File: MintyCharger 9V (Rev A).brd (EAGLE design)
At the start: 41.9 x 51.7 mm, 32 parts, among them IC1 PIC12F683P, IC2 7805L, IC3 LM358N, Q1 2N3904, Q2 2N3904, Q3 BD139

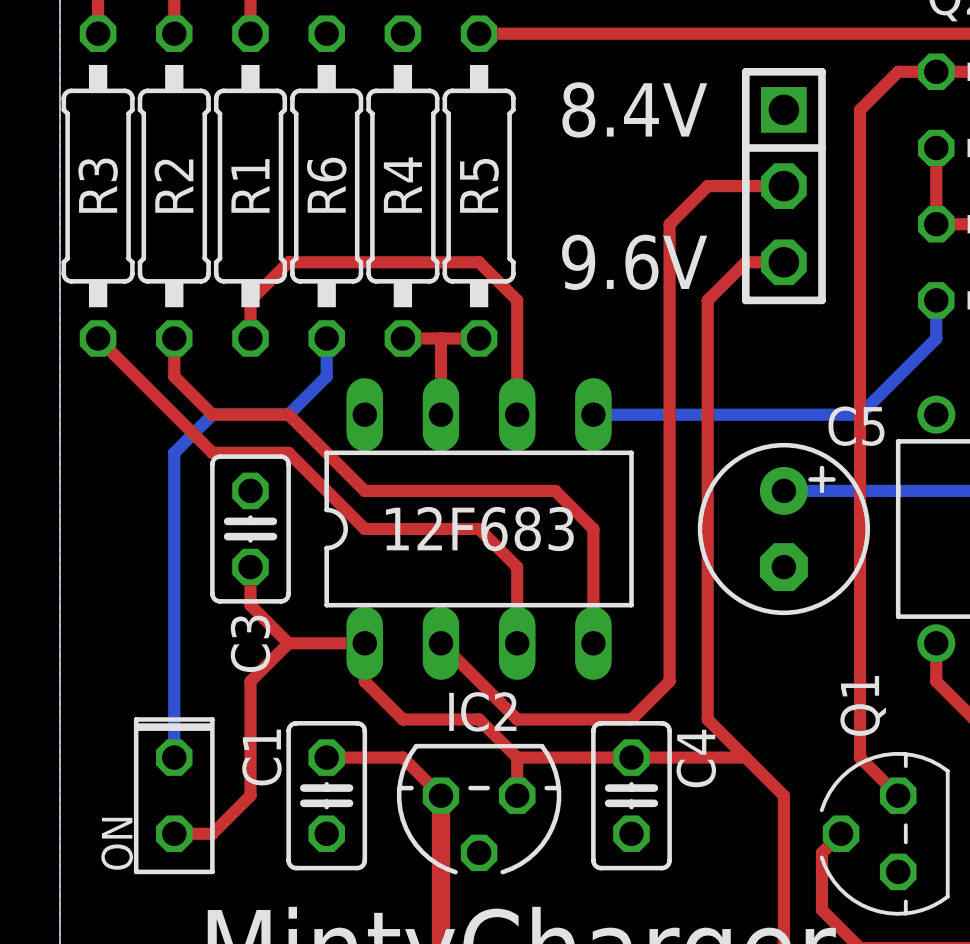
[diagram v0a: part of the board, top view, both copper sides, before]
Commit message: Moved BATT_SEL to GP3
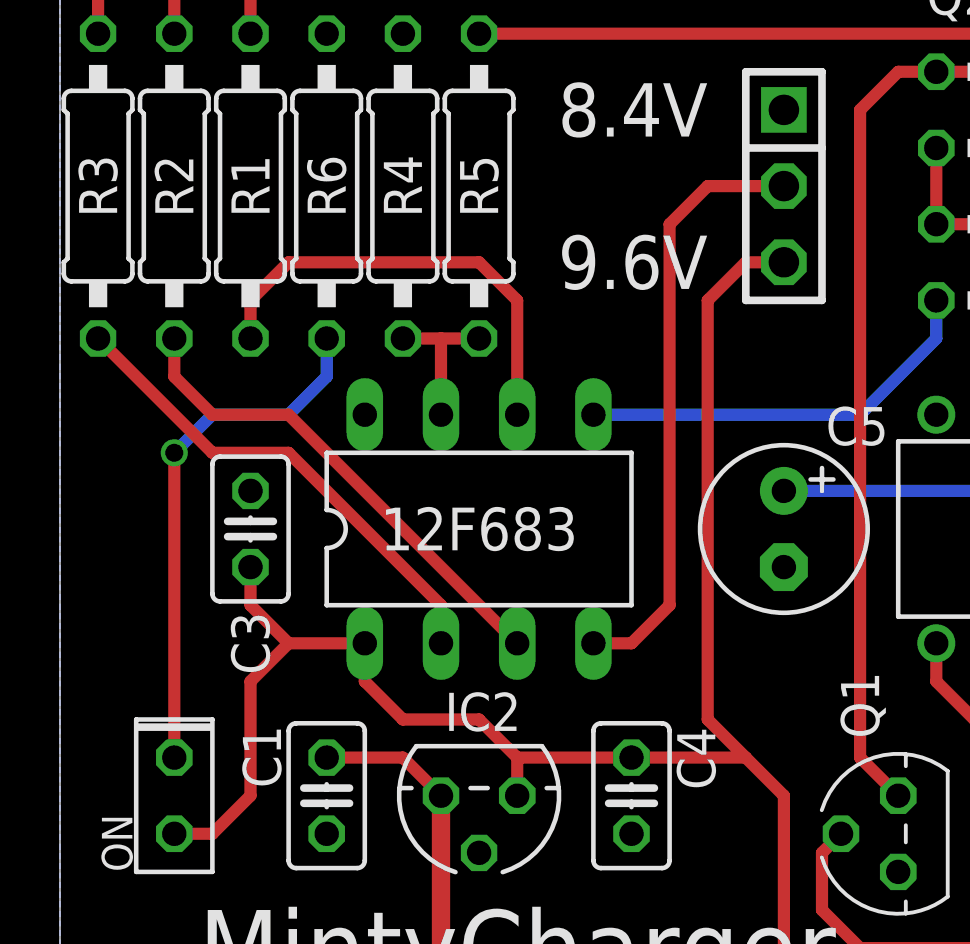
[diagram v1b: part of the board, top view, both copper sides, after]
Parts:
- VIN: value (none) -> 15V
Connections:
- net BATT_LVL2: now also IC1.3; no longer IC1.4
- net BATT_LVL3: now also IC1.2; no longer IC1.3
- net BATT_SEL: now also IC1.4; no longer IC1.2
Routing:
- net BATT_SEL: track 28.8 -> 20.1 mm
- net BATT_LVL2: track 21.2 -> 16.4 mm
- net BATT_LVL3: track 19.7 -> 16.4 mm
- net N$22: vias 0 -> 1
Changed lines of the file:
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@@
 <element name="C4" library="rcl" package="C025-025X050" value="100nF" x="19.05" y="11.43" rot="R270"/>
 <element name="BATT" library="adafruit" package="JST-PH-2-THM" value="" x="34.29" y="48.26" rot="R270"/>
-<element name="VIN" library="adafruit" package="JST-PH-2-THM" value="" x="25.4" y="45.72" rot="R180"/>
+<element name="VIN" library="adafruit" package="JST-PH-2-THM" value="15V" x="25.4" y="45.72" rot="R180"/>
 <element name="D2" library="diode" package="DO35-7" value="1N4148DO35-7" x="34.29" y="2.54" smashed="yes">
 <attribute name="NAME" x="27.94" y="2.54" size="1.27" layer="25" ratio="10" rot="R180" align="center"/>
@@
 <wire x1="7.62" y1="24.13" x2="5.08" y2="24.13" width="0.4064" layer="16"/>
 <wire x1="5.08" y1="24.13" x2="3.81" y2="22.86" width="0.4064" layer="16"/>
-<wire x1="3.81" y1="22.86" x2="3.81" y2="12.7" width="0.4064" layer="16"/>
+<wire x1="3.81" y1="12.7" x2="3.81" y2="22.86" width="0.4064" layer="1"/>
+<via x="3.81" y="22.86" extent="1-16" drill="0.6"/>
 </signal>
 <signal name="V+">
@@
 <signal name="BATT_SEL">
 <contactref element="SW_VBATT" pad="2"/>
-<contactref element="IC1" pad="2"/>
-<wire x1="20.32" y1="30.48" x2="20.32" y2="15.24" width="0.4064" layer="1"/>
-<wire x1="20.32" y1="15.24" x2="19.05" y2="13.97" width="0.4064" layer="1"/>
-<wire x1="19.05" y1="13.97" x2="15.24" y2="13.97" width="0.4064" layer="1"/>
-<wire x1="15.24" y1="13.97" x2="12.7" y2="16.51" width="0.4064" layer="1"/>
-<wire x1="24.13" y1="31.75" x2="21.59" y2="31.75" width="0.4064" layer="1"/>
-<wire x1="21.59" y1="31.75" x2="20.32" y2="30.48" width="0.4064" layer="1"/>
+<contactref element="IC1" pad="4"/>
+<wire x1="17.78" y1="16.51" x2="19.05" y2="16.51" width="0.4064" layer="1"/>
+<wire x1="19.05" y1="16.51" x2="20.32" y2="17.78" width="0.4064" layer="1"/>
+<wire x1="20.32" y1="17.78" x2="20.32" y2="30.48" width="0.4064" layer="1"/>
+<wire x1="20.32" y1="30.48" x2="21.59" y2="31.75" width="0.4064" layer="1"/>
+<wire x1="21.59" y1="31.75" x2="24.13" y2="31.75" width="0.4064" layer="1"/>
 </signal>
 <signal name="N$9">
@@
 </signal>
 <signal name="BATT_LVL2">
-<contactref element="IC1" pad="4"/>
 <contactref element="R2" pad="2"/>
 <wire x1="3.81" y1="26.67" x2="3.81" y2="25.4" width="0.4064" layer="1"/>
 <wire x1="3.81" y1="25.4" x2="5.08" y2="24.13" width="0.4064" layer="1"/>
 <wire x1="5.08" y1="24.13" x2="7.62" y2="24.13" width="0.4064" layer="1"/>
-<wire x1="7.62" y1="24.13" x2="10.16" y2="21.59" width="0.4064" layer="1"/>
-<wire x1="10.16" y1="21.59" x2="16.51" y2="21.59" width="0.4064" layer="1"/>
-<wire x1="16.51" y1="21.59" x2="17.78" y2="20.32" width="0.4064" layer="1"/>
-<wire x1="17.78" y1="20.32" x2="17.78" y2="16.51" width="0.4064" layer="1"/>
+<contactref element="IC1" pad="3"/>
+<wire x1="7.62" y1="24.13" x2="15.24" y2="16.51" width="0.4064" layer="1"/>
 </signal>
 <signal name="BATT_LVL3">
-<contactref element="IC1" pad="3"/>
 <contactref element="R3" pad="2"/>
 <wire x1="1.27" y1="26.67" x2="5.08" y2="22.86" width="0.4064" layer="1"/>
 <wire x1="5.08" y1="22.86" x2="7.62" y2="22.86" width="0.4064" layer="1"/>
-<wire x1="7.62" y1="22.86" x2="10.16" y2="20.32" width="0.4064" layer="1"/>
-<wire x1="10.16" y1="20.32" x2="13.97" y2="20.32" width="0.4064" layer="1"/>
-<wire x1="13.97" y1="20.32" x2="15.24" y2="19.05" width="0.4064" layer="1"/>
-<wire x1="15.24" y1="19.05" x2="15.24" y2="16.51" width="0.4064" layer="1"/>
+<contactref element="IC1" pad="2"/>
+<wire x1="7.62" y1="22.86" x2="12.7" y2="17.78" width="0.4064" layer="1"/>
+<wire x1="12.7" y1="17.78" x2="12.7" y2="16.51" width="0.4064" layer="1"/>
 </signal>
 <signal name="N$10">
